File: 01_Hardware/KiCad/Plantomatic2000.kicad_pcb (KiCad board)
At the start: 2 copper layers, 110 x 45 mm, 164 parts, among them J101 Conn_02x05_Odd_Even, J102 Conn_02x03_Odd_Even, J103 USB_C_Receptacle_USB2.0_16P, J105 JST_B4B, J106 Line Select, J107 Manual Start, J108 Hour, J109 Minute, J110 JST_4B4, J111 System Reset, J112 JST_B2B, J113 JST_B2B, J114 System Wake Up, J115 Running LED, J116 JST_4B4, Q101 IRLL014NP, Q102 IRLL014NP, Q104 NVTA7002NT1G, Q105 RU1E002SPTCL, Q106 NVTA7002NT1G, Q107 NVTA7002NT1G, Q108 RU1E002SPTCL, Q109 NVTA7002NT1G, Q110 RU1E002SPTCL, Q111 DTC143Z, Q112 DTC143Z, Q113 CSD17313Q2, SW102 SW_Push, SW103 SW_Push, U101 XC6220B331MR, U102 nPM1300, U103 ESP32-WROOM-32E, U104 TPS61287, U105 USBLC6-2P6, U106 CP2102N-A02-GQFN24, U107 DS3231M, U108 AT24CS01-SSHM

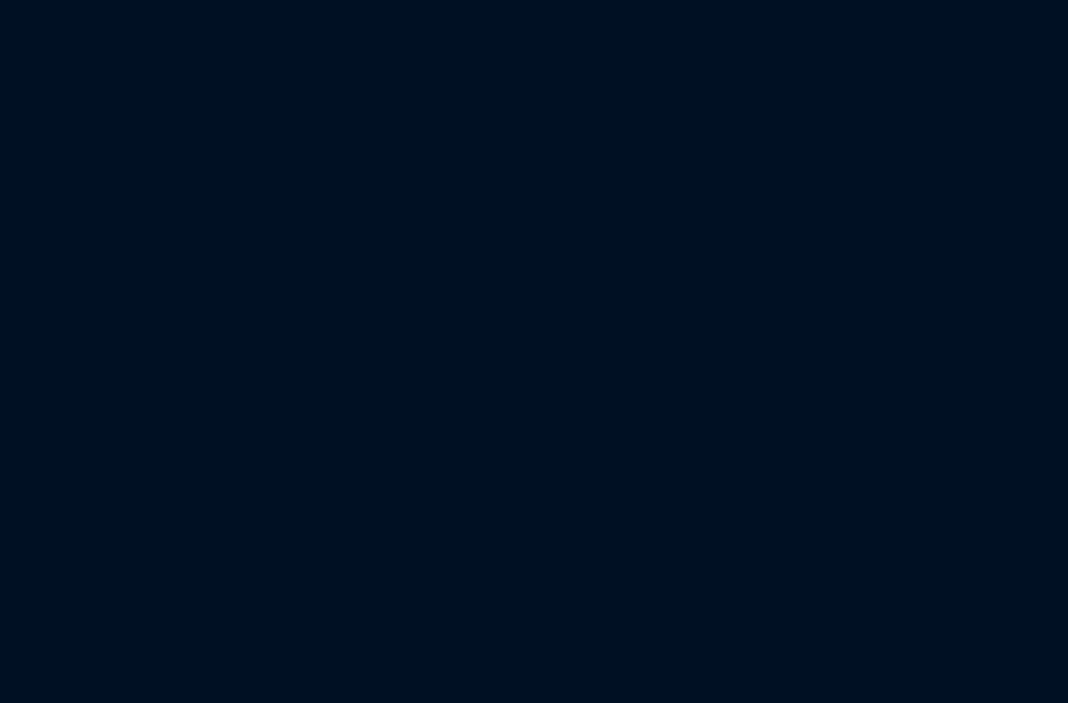
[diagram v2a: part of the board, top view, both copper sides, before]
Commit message: Added test points and schematic.pdf file
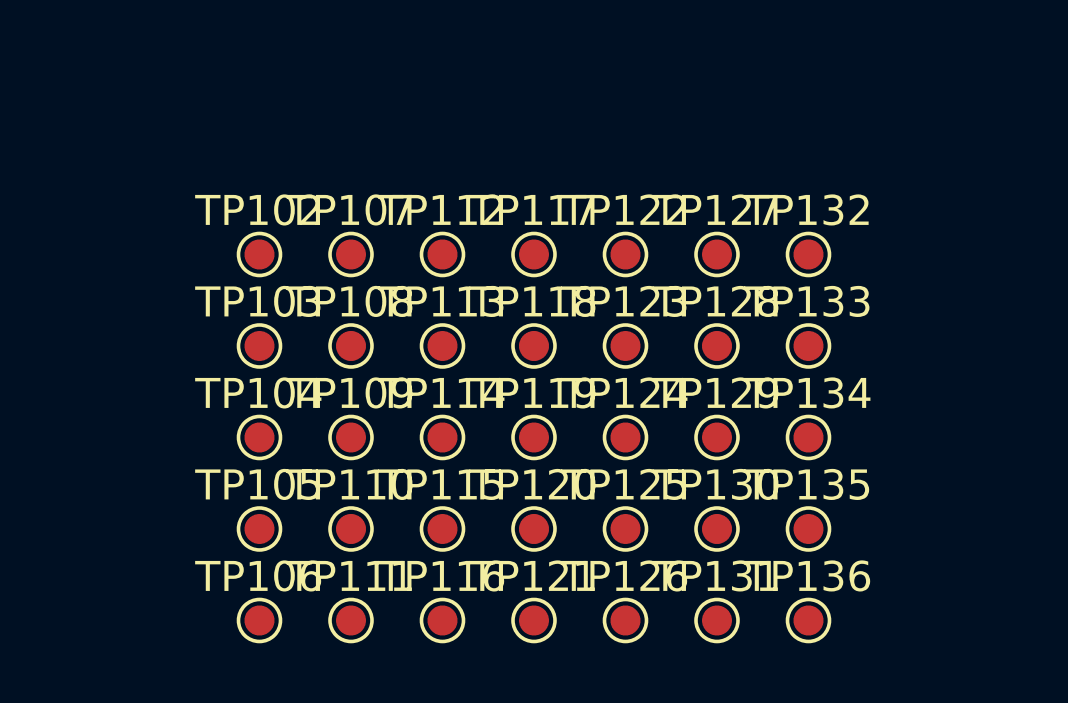
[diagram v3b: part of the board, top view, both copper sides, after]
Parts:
- added TP102: ~, TestPoint:TestPoint_Pad_D1.0mm, F.Cu at (192.7, 135.8)
- added TP103: ~, TestPoint:TestPoint_Pad_D1.0mm, F.Cu at (192.7, 138.8)
- added TP104: ~, TestPoint:TestPoint_Pad_D1.0mm, F.Cu at (192.7, 141.9)
- added TP105: ~, TestPoint:TestPoint_Pad_D1.0mm, F.Cu at (192.7, 144.9)
- added TP106: ~, TestPoint:TestPoint_Pad_D1.0mm, F.Cu at (192.7, 148.0)
- added TP107: ~, TestPoint:TestPoint_Pad_D1.0mm, F.Cu at (195.8, 135.8)
- added TP108: ~, TestPoint:TestPoint_Pad_D1.0mm, F.Cu at (195.8, 138.8)
- added TP109: ~, TestPoint:TestPoint_Pad_D1.0mm, F.Cu at (195.8, 141.9)
- added TP110: ~, TestPoint:TestPoint_Pad_D1.0mm, F.Cu at (195.8, 144.9)
- added TP111: ~, TestPoint:TestPoint_Pad_D1.0mm, F.Cu at (195.8, 148.0)
- added TP112: ~, TestPoint:TestPoint_Pad_D1.0mm, F.Cu at (198.8, 135.8)
- added TP113: ~, TestPoint:TestPoint_Pad_D1.0mm, F.Cu at (198.8, 138.8)
- added TP114: ~, TestPoint:TestPoint_Pad_D1.0mm, F.Cu at (198.8, 141.9)
- added TP115: ~, TestPoint:TestPoint_Pad_D1.0mm, F.Cu at (198.8, 144.9)
- added TP116: ~, TestPoint:TestPoint_Pad_D1.0mm, F.Cu at (198.8, 148.0)
- added TP117: ~, TestPoint:TestPoint_Pad_D1.0mm, F.Cu at (201.8, 135.8)
- added TP118: ~, TestPoint:TestPoint_Pad_D1.0mm, F.Cu at (201.8, 138.8)
- added TP119: ~, TestPoint:TestPoint_Pad_D1.0mm, F.Cu at (201.8, 141.9)
- added TP120: ~, TestPoint:TestPoint_Pad_D1.0mm, F.Cu at (201.8, 144.9)
- added TP121: ~, TestPoint:TestPoint_Pad_D1.0mm, F.Cu at (201.8, 148.0)
- added TP122: ~, TestPoint:TestPoint_Pad_D1.0mm, F.Cu at (204.9, 135.8)
- added TP123: ~, TestPoint:TestPoint_Pad_D1.0mm, F.Cu at (204.9, 138.8)
- added TP124: ~, TestPoint:TestPoint_Pad_D1.0mm, F.Cu at (204.9, 141.9)
- added TP125: ~, TestPoint:TestPoint_Pad_D1.0mm, F.Cu at (204.9, 144.9)
- added TP126: ~, TestPoint:TestPoint_Pad_D1.0mm, F.Cu at (204.9, 148.0)
- added TP127: ~, TestPoint:TestPoint_Pad_D1.0mm, F.Cu at (207.9, 135.8)
- added TP128: ~, TestPoint:TestPoint_Pad_D1.0mm, F.Cu at (207.9, 138.8)
- added TP129: ~, TestPoint:TestPoint_Pad_D1.0mm, F.Cu at (207.9, 141.9)
- added TP130: ~, TestPoint:TestPoint_Pad_D1.0mm, F.Cu at (207.9, 144.9)
- added TP131: ~, TestPoint:TestPoint_Pad_D1.0mm, F.Cu at (207.9, 148.0)
- added TP132: ~, TestPoint:TestPoint_Pad_D1.0mm, F.Cu at (211.0, 135.8)
- added TP133: ~, TestPoint:TestPoint_Pad_D1.0mm, F.Cu at (211.0, 138.8)
- added TP134: ~, TestPoint:TestPoint_Pad_D1.0mm, F.Cu at (211.0, 141.9)
- added TP135: ~, TestPoint:TestPoint_Pad_D1.0mm, F.Cu at (211.0, 144.9)
- added TP136: ~, TestPoint:TestPoint_Pad_D1.0mm, F.Cu at (211.0, 148.0)
- R139: value 470R -> 1K
- R148, R149, R150: value 220R -> 1K

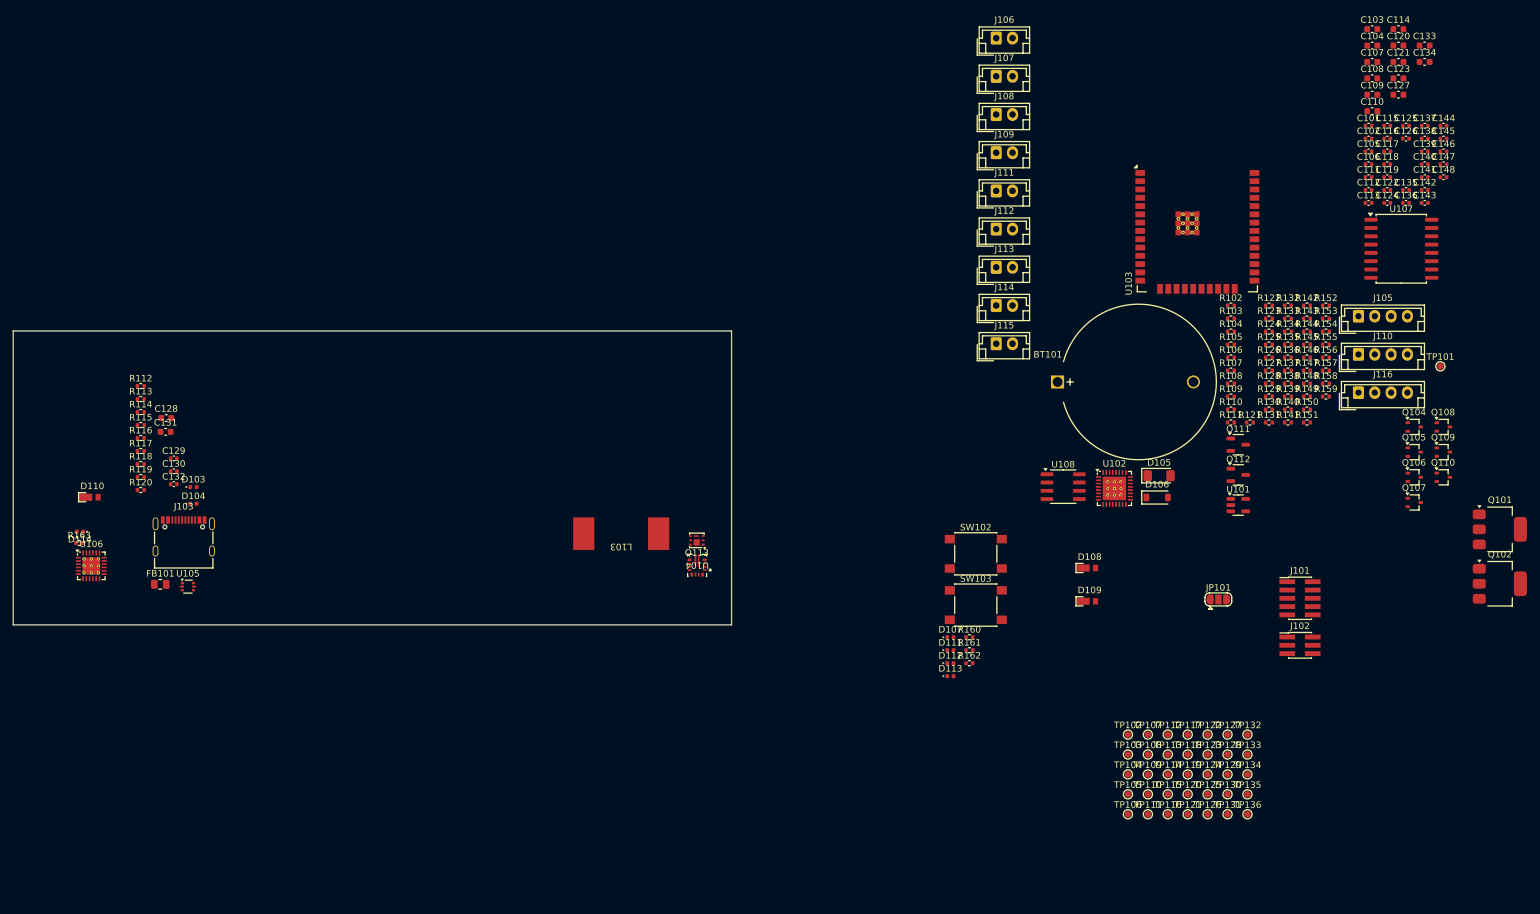
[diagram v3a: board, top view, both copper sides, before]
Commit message: PCB layout BOOST converter
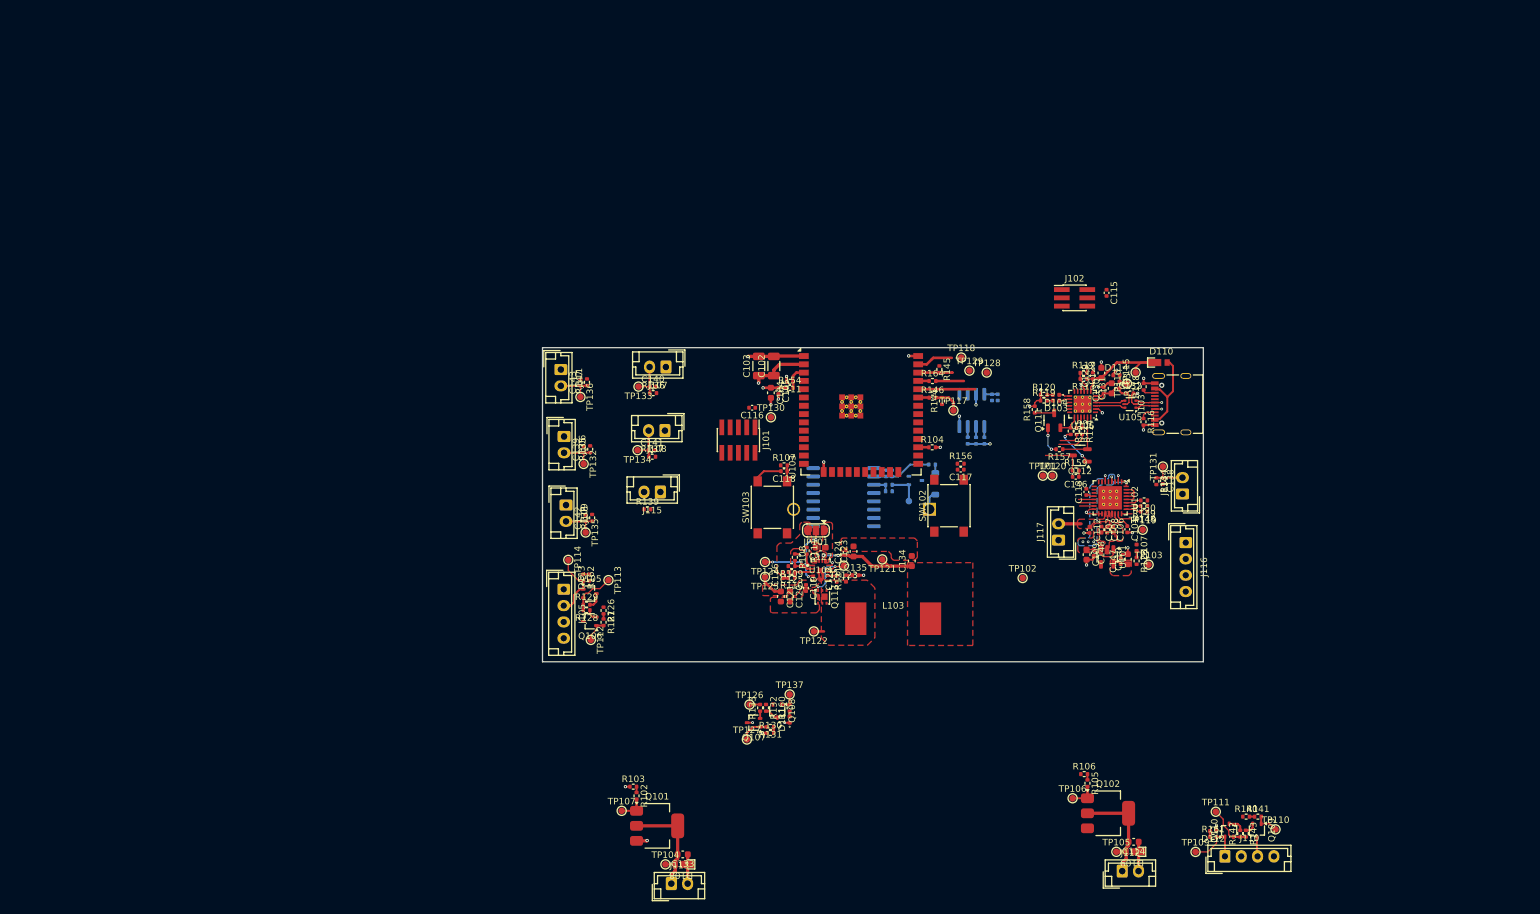
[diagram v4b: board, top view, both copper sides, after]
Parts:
- removed D105: UCLAMP6061P.TNT, Diode_SMD:D_MiniMELF
- removed FB101: MH2029-300Y, Resistor_SMD:R_0805_2012Metric
- added G***: LOGO, Custom_Global_Footprints:Italdesigh_13_Logo, B.Cu at (401.6, 225.9)
- added J117: Running LED, Connector_JST:JST_EH_B2B-EH-A_1x02_P2.50mm_Vertical, F.Cu at (182.1, 106.0)
- added R164: 0R, Resistor_SMD:R_0402_1005Metric, F.Cu at (162.8, 81.7)
- added TP137: ~, TestPoint:TestPoint_Pad_D1.0mm, F.Cu at (140.9, 129.7)
- BT101, C136, C137, C144, C145, D106, Q104, R112, R122, R124, R125, R151, R152, R153, TP108, U107, U108: moved to B.Cu
- C102: value 100nF -> 100nF tantulum; footprint Capacitor_SMD:C_0402_1005Metric -> Capacitor_SMD:C_1206_3216Metric
- C103: value 10uF -> 10uF tantulum; footprint Capacitor_SMD:C_0603_1608Metric -> Capacitor_SMD:C_1206_3216Metric
- C107, C108: footprint Capacitor_SMD:C_0603_1608Metric -> Capacitor_SMD:C_0402_1005Metric
- R114, R115: value 470R -> 0R
- moved C133 168.1 mm to (124.5, 154.2), turned to 180 degrees
- moved D110 165.0 mm to (197.8, 78.8)
- moved R163 161.1 mm to (191.4, 82.2), turned to -90 degrees
- moved D114 160.5 mm to (190.9, 80.8), turned to 0 degrees
- moved R118 154.0 mm to (195.1, 82.5), turned to 90 degrees
- moved U106 153.8 mm to (185.8, 85.2), turned to 180 degrees
- moved R116 153.6 mm to (195.1, 87.9), turned to -90 degrees
- moved J103 152.6 mm to (199.3, 85.2), turned to 90 degrees
- moved C132 147.1 mm to (193.1, 83.5)
- moved U105 147.0 mm to (193.1, 85.2), turned to 180 degrees
- moved R112 145.4 mm to (186.9, 81.3), turned to 180 degrees
- moved C131 145.0 mm to (190.2, 82.8), turned to 90 degrees
- moved R117 144.9 mm to (185.9, 80.4)
- moved R113 144.4 mm to (185.9, 81.3), turned to 180 degrees
- moved R114 144.2 mm to (185.7, 89.3), turned to -90 degrees
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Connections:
- net Net-(JP101-A) renamed /CVCC
- C122 pad 1: Net-(U104-SW) -> /SW
- J103 pad S1: /SHIELD -> unconnected-(J103-SHIELD-PadS1)_3
- L103 pad 1: +VSYS -> /SW
- L103 pad 2: Net-(U104-SW) -> +VSYS
- Q112 pad 2: GND -> /DTR_SERIAL
- Q113 pad 1: Net-(U104-SW) -> /SW
- Q113 pad 2: Net-(U104-SW) -> /SW
- Q113 pad 5: Net-(U104-SW) -> /SW
- Q113 pad 6: Net-(U104-SW) -> /SW
- Q113 pad 8: Net-(U104-SW) -> /SW
- R121 pad 1: Net-(U104-SW) -> /SW
- R157 pad 1: GND -> /DTR_SERIAL
- TP122 pad 1: Net-(U104-SW) -> /SW
- U103 pad 35: /ESP_TX -> Net-(U103-TXD0/IO1)
- U104 pad 6: Net-(U104-SW) -> /SW
- U106 pad 23: GND -> /DTR_SERIAL
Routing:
- net GND: track 0.00 -> 67.2 mm, vias 0 -> 33
- net +3V3: track 0.00 -> 32.0 mm, vias 0 -> 4
- net +VSYS: track 0.00 -> 30.0 mm, vias 0 -> 7
- net Net-(D109-A): track 0.00 -> 17.1 mm
- net Net-(D108-A): track 0.00 -> 17.1 mm
- net VBUS: track 0.00 -> 16.3 mm
- net +12V: track 0.00 -> 16.1 mm, vias 0 -> 1
- net VDD: track 0.00 -> 15.3 mm, vias 0 -> 2
- net /ESP_RX: track 0.00 -> 13.3 mm
- net /VBUSD: track 0.00 -> 13.3 mm
- net Net-(J105-Pin_2): track 0.00 -> 10.5 mm
- net Net-(U104-FB): track 0.00 -> 10.2 mm, vias 0 -> 2
- net Net-(JP101-C): track 0.00 -> 9.06 mm, vias 0 -> 2
- net Net-(J110-Pin_1): track 0.00 -> 9.02 mm
- net /DTR_SERIAL: track 0.00 -> 8.71 mm
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- added copper zone on F.Cu, net +12V
- added copper zone on F.Cu, net +3V3
- added copper zone on F.Cu, net +VBAT
- added copper zone on B.Cu, net +VSYS
- added copper zone on F.Cu, net +VSYS
- added copper zone on F.Cu, net /CVCC
- added copper zone on F.Cu, net /SW
- added copper zone on F.Cu, net GND
- added copper zone on In1.Cu, net GND
- added copper zone on In2.Cu, net GND
- added copper zone on F.Cu, net VBUS
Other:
- board size 110 x 45 mm -> 101.2 x 48.1 mm
- copper layers 2 -> 4

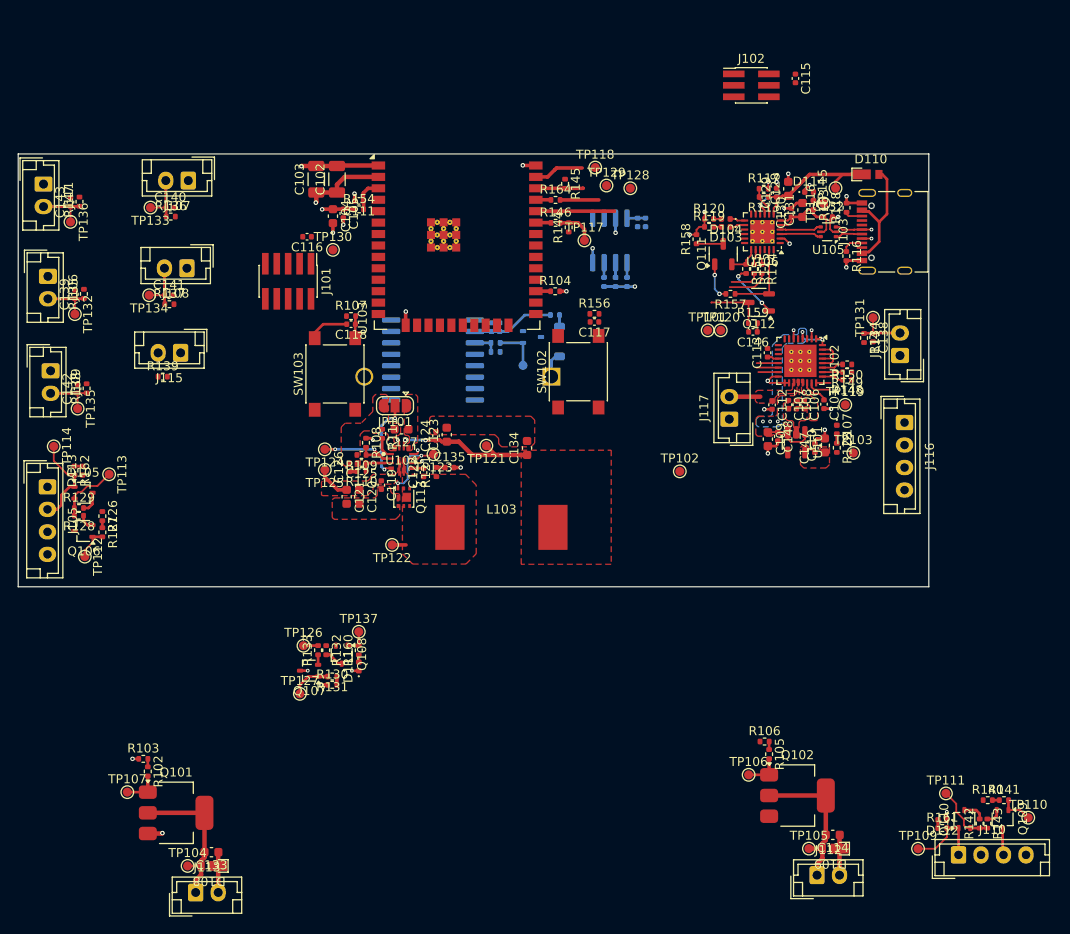
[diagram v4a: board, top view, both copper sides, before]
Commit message: PCB design continued -> Top layer mainly routed/ bottom layer GND pour and minor routing left to do + mounting holes
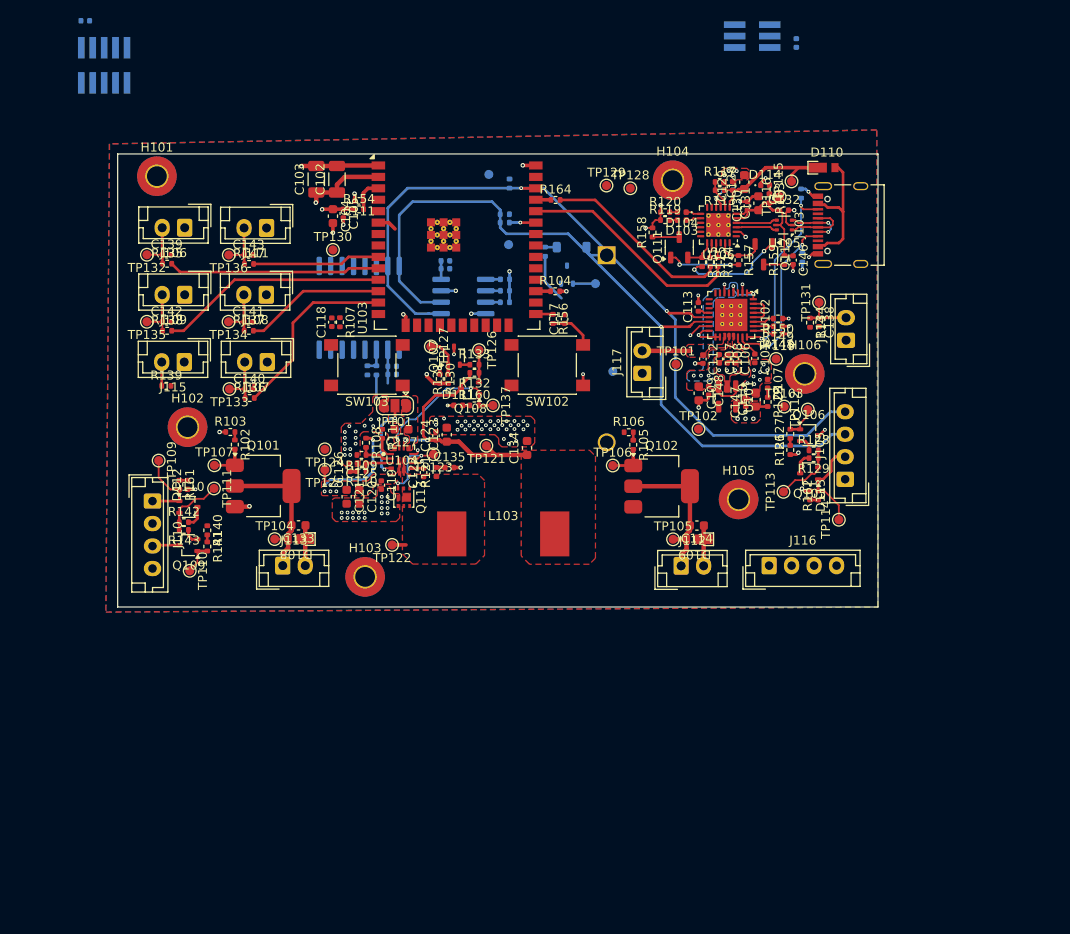
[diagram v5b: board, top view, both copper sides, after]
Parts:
- added H101: MountingHole_Pad, MountingHole:MountingHole_2.2mm_M2_Pad_TopBottom, F.Cu at (118.5, 79.0)
- added H102: MountingHole_Pad, MountingHole:MountingHole_2.2mm_M2_Pad_TopBottom, F.Cu at (121.9, 106.9)
- added H103: MountingHole_Pad, MountingHole:MountingHole_2.2mm_M2_Pad_TopBottom, F.Cu at (141.6, 123.5)
- added H104: MountingHole_Pad, MountingHole:MountingHole_2.2mm_M2_Pad_TopBottom, F.Cu at (175.8, 79.5)
- added H105: MountingHole_Pad, MountingHole:MountingHole_2.2mm_M2_Pad_TopBottom, F.Cu at (183.1, 114.9)
- added H106: MountingHole_Pad, MountingHole:MountingHole_2.2mm_M2_Pad_TopBottom, F.Cu at (190.5, 101.0)
- C115, C116, J101, J102, R116, R118, R144, R145, R146, TP117, TP118, TP120: moved to B.Cu
- moved J110 97.8 mm to (118.0, 115.1), turned to -90 degrees
- moved TP110 97.1 mm to (122.1, 122.9), turned to -90 degrees
- moved Q109 95.5 mm to (122.0, 120.0), turned to 180 degrees
- moved R143 95.1 mm to (121.5, 118.3), turned to 180 degrees
- moved TP109 94.8 mm to (118.7, 110.6), turned to -90 degrees
- moved R142 94.6 mm to (121.5, 117.5), turned to 0 degrees
- moved R161 93.0 mm to (121.0, 113.3), turned to -90 degrees
- moved Q110 93.0 mm to (122.0, 115.8), turned to 0 degrees
- moved R141 92.9 mm to (124.1, 120.2), turned to -90 degrees
- moved D112 91.8 mm to (121.9, 113.3), turned to 90 degrees
- moved R140 91.8 mm to (124.1, 118.4), turned to -90 degrees
- moved J105 88.7 mm to (194.9, 112.7), turned to 90 degrees
- moved TP111 88.1 mm to (124.8, 113.7), turned to -90 degrees
- moved TP114 87.6 mm to (194.2, 117.2), turned to 90 degrees
- moved R162 82.7 mm to (191.9, 114.5), turned to 90 degrees
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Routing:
- net SDA: track 7.65 -> 91.8 mm, vias 0 -> 2
- net SCL: track 6.64 -> 86.7 mm, vias 0 -> 1
- net MIN_BUTTON_PIN: track 0.00 -> 25.3 mm
- net SELECT_LINE_BUTTON_PIN: track 0.00 -> 23.5 mm
- net START_BUTTON_PIN: track 0.00 -> 20.6 mm
- net /USB_CC2_PD: track 3.60 -> 21.6 mm, vias 0 -> 2
- net HOUR_BUTTON_PIN: track 0.00 -> 15.7 mm
- net /USB_CC1_PD: track 5.05 -> 19.9 mm, vias 0 -> 2
- net RESET_BUTTON_PIN: track 0.00 -> 14.2 mm
- net /ESP_TX: track 7.52 -> 21.0 mm
- net Net-(Q108-D): track 3.72 -> 16.2 mm, vias 1 -> 2
- net /ESP_RX: track 13.3 -> 25.1 mm
- net +12V: track 16.1 -> 23.5 mm, vias 1 -> 7
- net +VSYS: track 30.0 -> 36.7 mm
- net Net-(U104-FB): track 10.2 -> 3.80 mm, vias 2 -> 0
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- added copper zone on B.Cu, net GND
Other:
- board size 101.2 x 48.1 mm -> 84.5 x 50.4 mm
